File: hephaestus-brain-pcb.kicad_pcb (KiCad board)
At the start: 2 copper layers, 19.1 x 64.8 mm, 10 parts, among them J1 Barrel_Jack, J2 ItsyBitsy, J3 ItsyBitsy, J4 Conn_01x03_Male, J5 Conn_01x03_Male, J6 Conn_01x03_Male, J7 Conn_01x03_Male, U1 74126

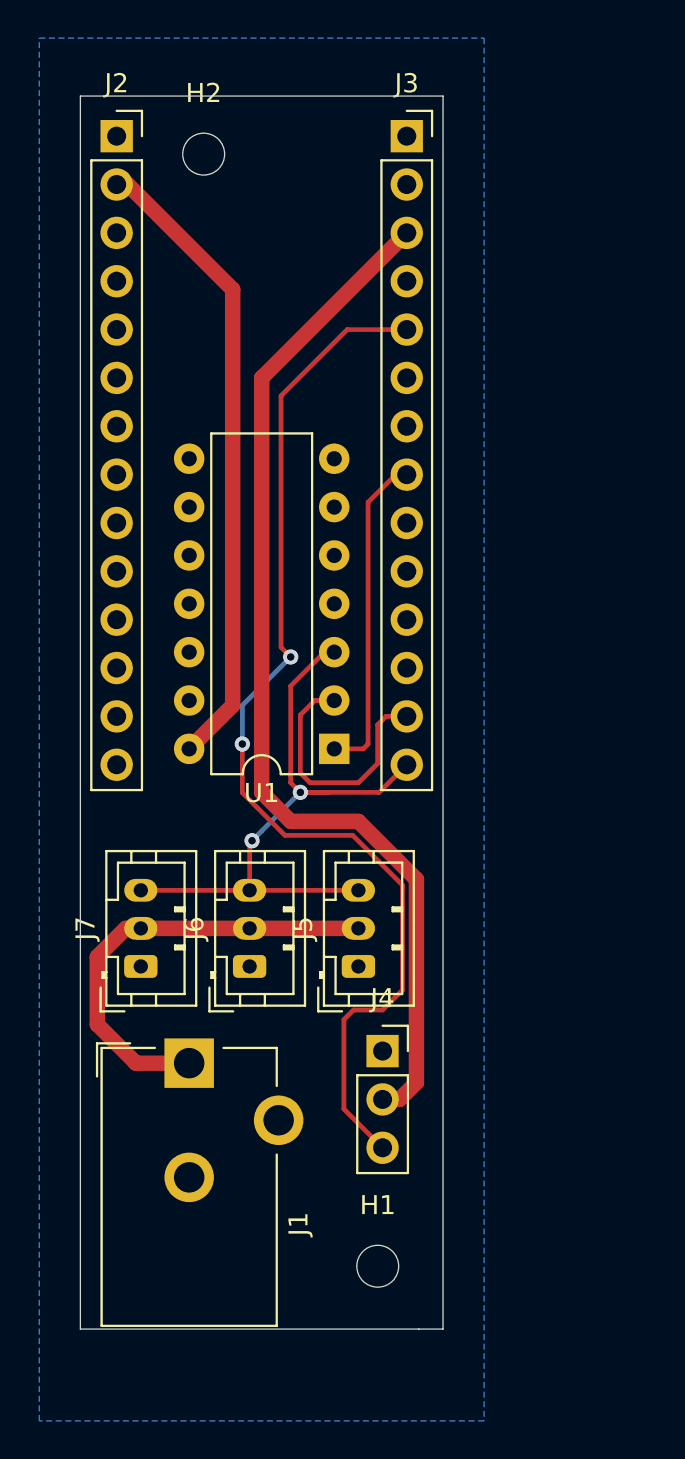
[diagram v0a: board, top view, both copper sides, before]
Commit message: Added homing switch connector
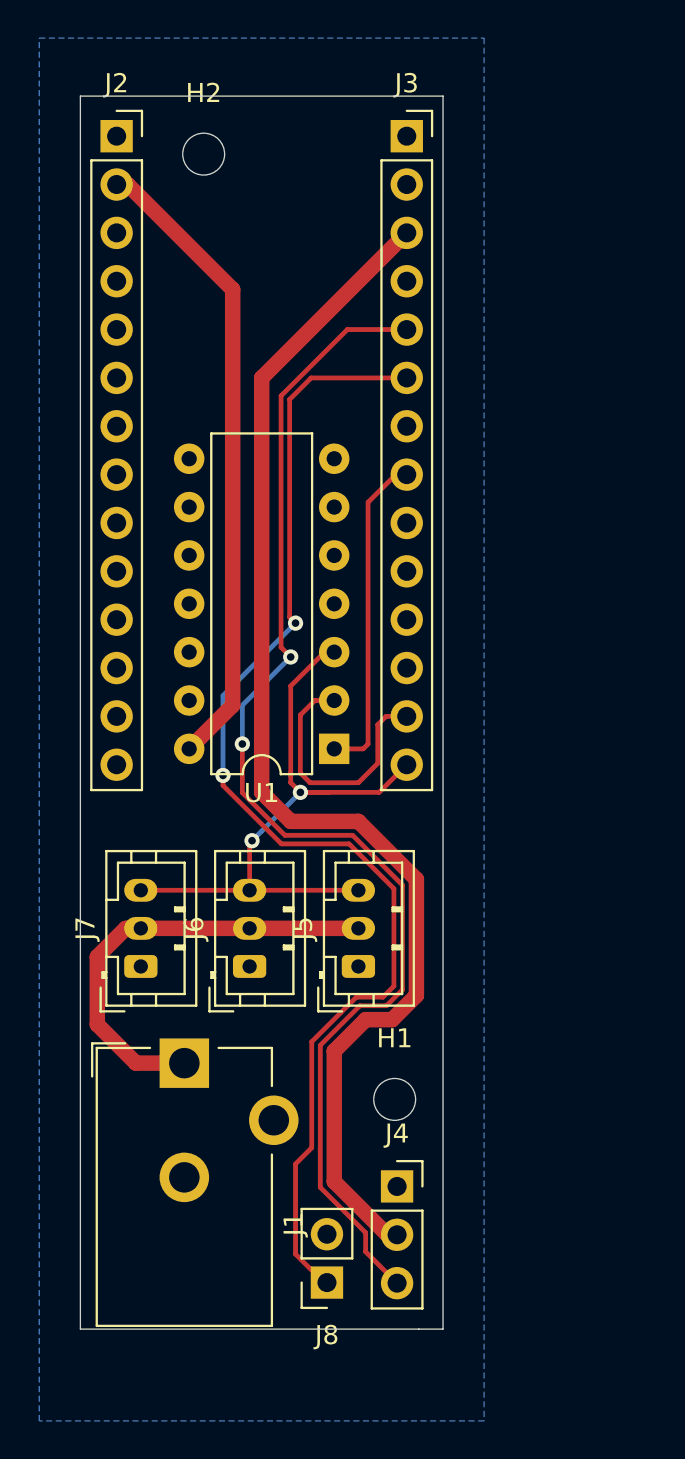
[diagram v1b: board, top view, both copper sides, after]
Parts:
- added J8: Conn_01x02_Female, Connector_PinSocket_2.54mm:PinSocket_1x02_P2.54mm_Vertical, F.Cu at (176.1, 123.3)
- moved H1 8.81 mm to (179.7, 113.7)
- moved J4 7.15 mm to (179.8, 118.2)
- moved J1 0.25 mm to (168.7, 111.8)
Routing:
- net 11: track 0.00 -> 64.3 mm, vias 0 -> 2
- net USB: track 55.4 -> 65.5 mm
- net 12: track 57.4 -> 65.8 mm

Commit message: Added switch, button.
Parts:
- added SW1: SW_SPDT, Button_Switch_THT:SW_Slide_1P2T_CK_OS102011MS2Q, F.Cu at (184.9, 70.6)
- added SW2: SW_SPST, Button_Switch_THT:SW_PUSH_6mm, F.Cu at (188.5, 77.3)
- added SW3: SW_SPST, Button_Switch_THT:SW_PUSH_6mm, F.Cu at (188.5, 87.0)
- J8: value Conn_01x02_Female -> Conn_01x03_Male; footprint Connector_PinSocket_2.54mm:PinSocket_1x02_P2.54mm_Vertical -> Connector_PinSocket_2.54mm:PinSocket_1x03_P2.54mm_Vertical
- moved J8 20.0 mm to (176.8, 103.3), turned to 90 degrees
- moved J4 18.9 mm to (176.8, 99.6), turned to 90 degrees
- moved H1 13.8 mm to (187.8, 102.5)
- moved J1 11.9 mm to (168.3, 99.8)
- moved J5 10.5 mm to (187.1, 111.6)
- moved J6 10.5 mm to (181.4, 111.6)
- moved J7 10.5 mm to (175.6, 111.6)
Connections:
- J8 pad 1: 11 -> GND
- J8 pad 2: GND -> USB
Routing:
- net 11: track 64.3 -> 4.54 mm, vias 2 -> 0
- net 13: track 0.00 -> 38.8 mm
- net 12: track 65.8 -> 32.7 mm, vias 2 -> 0
- net USB: track 65.5 -> 43.0 mm
- net 10: track 0.00 -> 16.4 mm
- net TX: track 13.6 -> 4.16 mm
- net RX: track 33.8 -> 42.8 mm, vias 2 -> 0
- net 9: track 17.2 -> 19.9 mm
- net VPOW: track 23.6 -> 25.5 mm
- net 3v: track 33.5 -> 34.2 mm
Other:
- board size 19.1 x 64.8 mm -> 27.3 x 53.1 mm

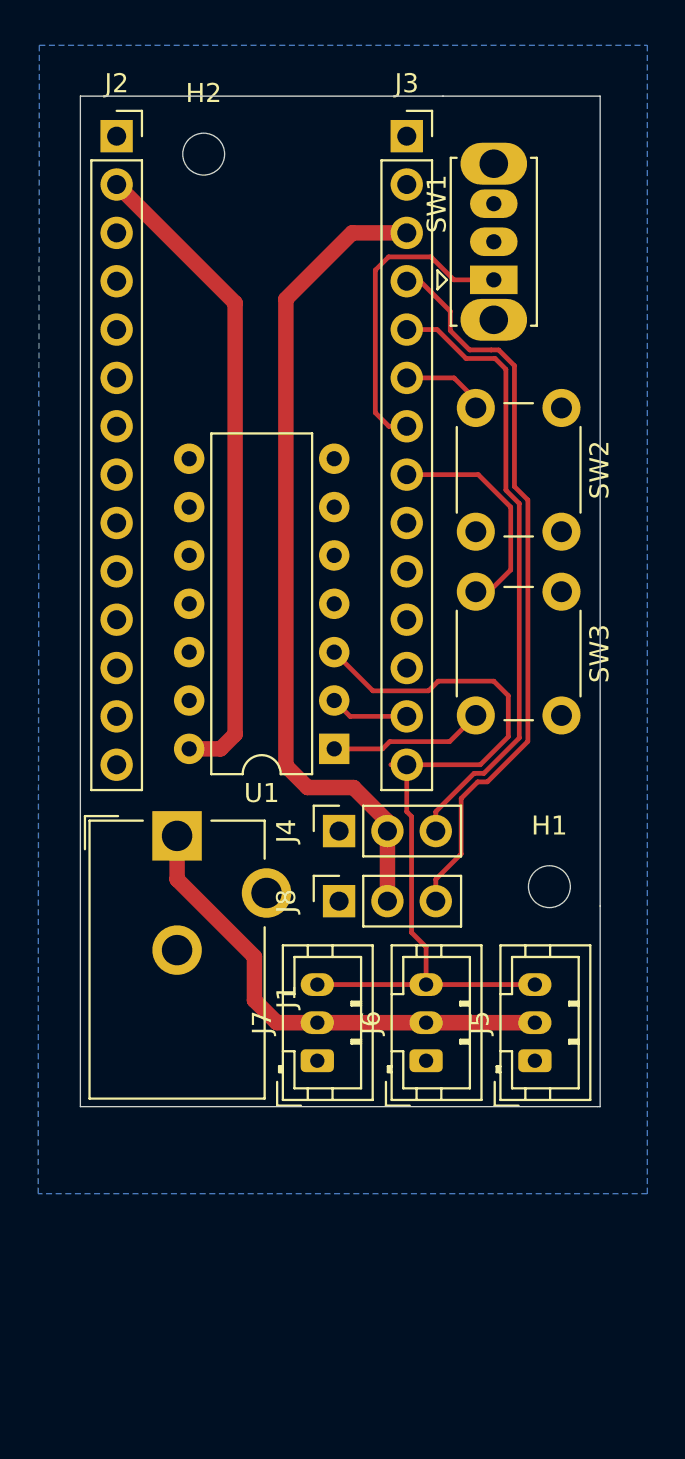
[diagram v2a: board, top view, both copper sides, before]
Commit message: Updated Silkscreen
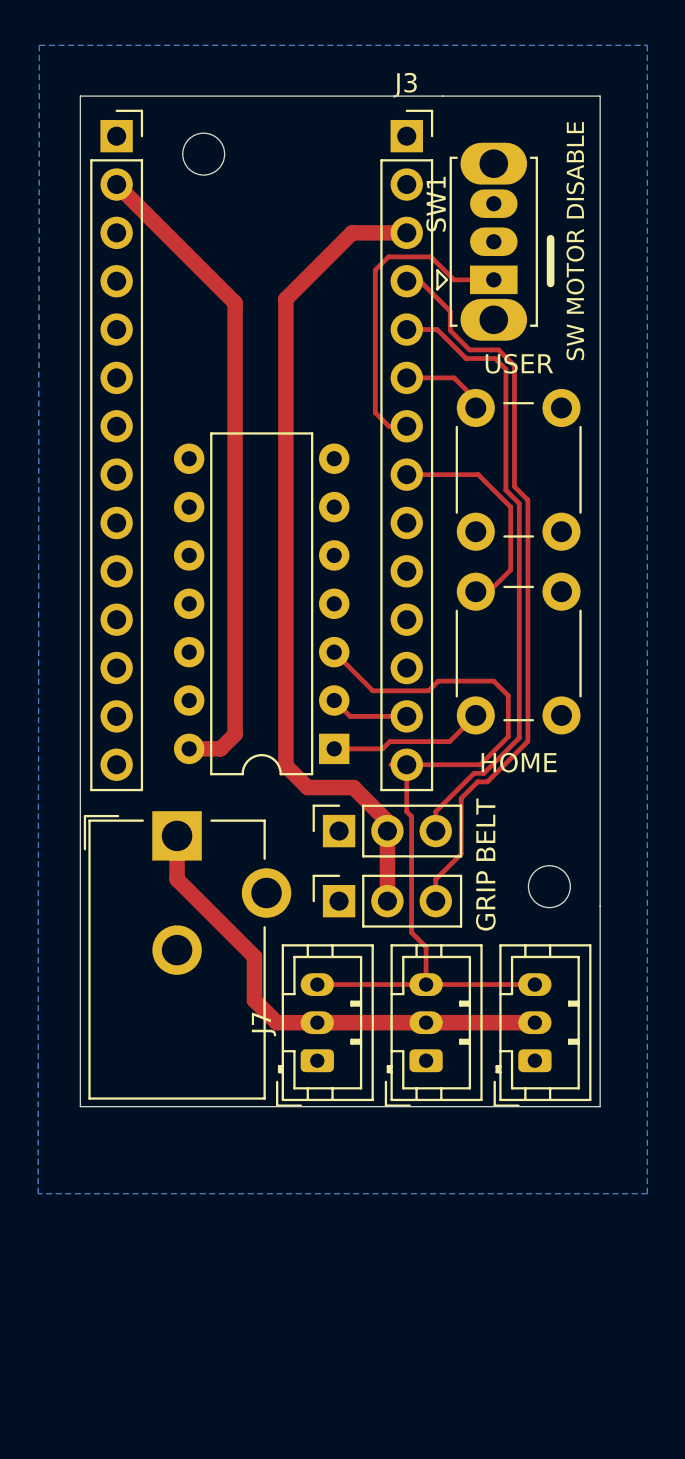
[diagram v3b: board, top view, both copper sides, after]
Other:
- board text added: "BELT"
- board text added: "GRIP"
- board text added: "HOME"
- board text added: "SW MOTOR DISABLE"
- board text added: "USER"
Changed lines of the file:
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@@
   (general
     (thickness 1.6)
-    (drawings 7)
+    (drawings 13)
     (tracks 83)
     (zones 0)
@@
     (descr "Thin-pin DC Barrel Jack, https://cdn-shop.adafruit.com/datasheets/21mmdcjackDatasheet.pdf")
     (tags "Power Jack")
-    (fp_text reference J1 (at 5.75 8.45 90) (layer F.SilkS)
+    (fp_text reference J1 (at 5.75 8.45 90) (layer F.SilkS) hide
       (effects (font (size 1 1) (thickness 0.15)))
     )
@@
     (descr "Through hole straight socket strip, 1x14, 2.54mm pitch, single row (from Kicad 4.0.7), script generated")
     (tags "Through hole socket strip THT 1x14 2.54mm single row")
-    (fp_text reference J2 (at 0 -2.77) (layer F.SilkS)
+    (fp_text reference J2 (at 0 -2.77) (layer F.SilkS) hide
       (effects (font (size 1 1) (thickness 0.15)))
     )
@@
     (descr "Through hole straight socket strip, 1x03, 2.54mm pitch, single row (from Kicad 4.0.7), script generated")
     (tags "Through hole socket strip THT 1x03 2.54mm single row")
-    (fp_text reference J4 (at 0 -2.77 90) (layer F.SilkS)
+    (fp_text reference J4 (at 0 -2.77 90) (layer F.SilkS) hide
       (effects (font (size 1 1) (thickness 0.15)))
     )
@@
     (descr "JST PH series connector, B3B-PH-K (http://www.jst-mfg.com/product/pdf/eng/ePH.pdf), generated with kicad-footprint-generator")
     (tags "connector JST PH side entry")
-    (fp_text reference J5 (at 2 -2.9 90) (layer F.SilkS)
+    (fp_text reference J5 (at 2 -2.9 90) (layer F.SilkS) hide
       (effects (font (size 1 1) (thickness 0.15)))
     )
@@
     (descr "JST PH series connector, B3B-PH-K (http://www.jst-mfg.com/product/pdf/eng/ePH.pdf), generated with kicad-footprint-generator")
     (tags "connector JST PH side entry")
-    (fp_text reference J6 (at 2 -2.9 90) (layer F.SilkS)
+    (fp_text reference J6 (at 2 -2.9 90) (layer F.SilkS) hide
       (effects (font (size 1 1) (thickness 0.15)))
     )
@@
     (descr "14-lead though-hole mounted DIP package, row spacing 7.62 mm (300 mils)")
     (tags "THT DIP DIL PDIP 2.54mm 7.62mm 300mil")
-    (fp_text reference U1 (at 3.81 -2.33) (layer F.SilkS)
+    (fp_text reference U1 (at 3.81 -2.33) (layer F.SilkS) hide
       (effects (font (size 1 1) (thickness 0.15)))
     )
@@
     (tags "mounting hole 2.2mm no annular m2")
     (attr virtual)
-    (fp_text reference H1 (at 0 -3.2) (layer F.SilkS)
+    (fp_text reference H1 (at 0 -3.2) (layer F.SilkS) hide
       (effects (font (size 1 1) (thickness 0.15)))
     )
@@
     (tags "mounting hole 2.2mm no annular m2")
     (attr virtual)
-    (fp_text reference H2 (at 0 -3.2) (layer F.SilkS)
+    (fp_text reference H2 (at 0 -3.2) (layer F.SilkS) hide
       (effects (font (size 1 1) (thickness 0.15)))
     )
@@
     (descr https://www.omron.com/ecb/products/pdf/en-b3f.pdf)
     (tags "tact sw push 6mm")
-    (fp_text reference SW2 (at 3.25 -2 90) (layer F.SilkS)
+    (fp_text reference SW2 (at 3.25 -2 90) (layer F.SilkS) hide
       (effects (font (size 1 1) (thickness 0.15)))
     )
@@
     (descr https://www.omron.com/ecb/products/pdf/en-b3f.pdf)
     (tags "tact sw push 6mm")
-    (fp_text reference SW3 (at 3.25 -2 90) (layer F.SilkS)
+    (fp_text reference SW3 (at 3.25 -2 90) (layer F.SilkS) hide
       (effects (font (size 1 1) (thickness 0.15)))
     )
@@
     (descr "Through hole straight socket strip, 1x03, 2.54mm pitch, single row (from Kicad 4.0.7), script generated")
     (tags "Through hole socket strip THT 1x03 2.54mm single row")
-    (fp_text reference J8 (at 0 -2.77 90) (layer F.SilkS)
+    (fp_text reference J8 (at 0 -2.77 90) (layer F.SilkS) hide
       (effects (font (size 1 1) (thickness 0.15)))
     )
@@
     )
   )
+  (gr_line (start 187.8965 68.453) (end 187.8965 70.8025) (layer F.SilkS) (width 0.4))
+  (gr_text "SW MOTOR DISABLE" (at 189.23 68.58 90) (layer F.SilkS)
+    (effects (font (size 0.9 0.9) (thickness 0.2)))
+  )
+  (gr_text USER (at 186.218 75.057) (layer F.SilkS)
+    (effects (font (size 1 1) (thickness 0.2)))
+  )
+  (gr_text BELT (at 184.531 99.568 90) (layer F.SilkS)
+    (effects (font (size 1 1) (thickness 0.2)))
+  )
+  (gr_text GRIP (at 184.531 103.251 90) (layer F.SilkS)
+    (effects (font (size 1 1) (thickness 0.2)))
+  )
+  (gr_text HOME (at 186.218 96.012) (layer F.SilkS)
+    (effects (font (size 1 1) (thickness 0.2)))
+  )
   (gr_line (start 163.195 114.046) (end 163.195 60.96) (layer Edge.Cuts) (width 0.05))
